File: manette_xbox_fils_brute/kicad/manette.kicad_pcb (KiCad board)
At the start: 2 copper layers, 100 x 53 mm, 25 parts, among them J1 THB001P, J2 THB001P, J3 Conn_01x20, X1 SW_Push, Y1 SW_Push

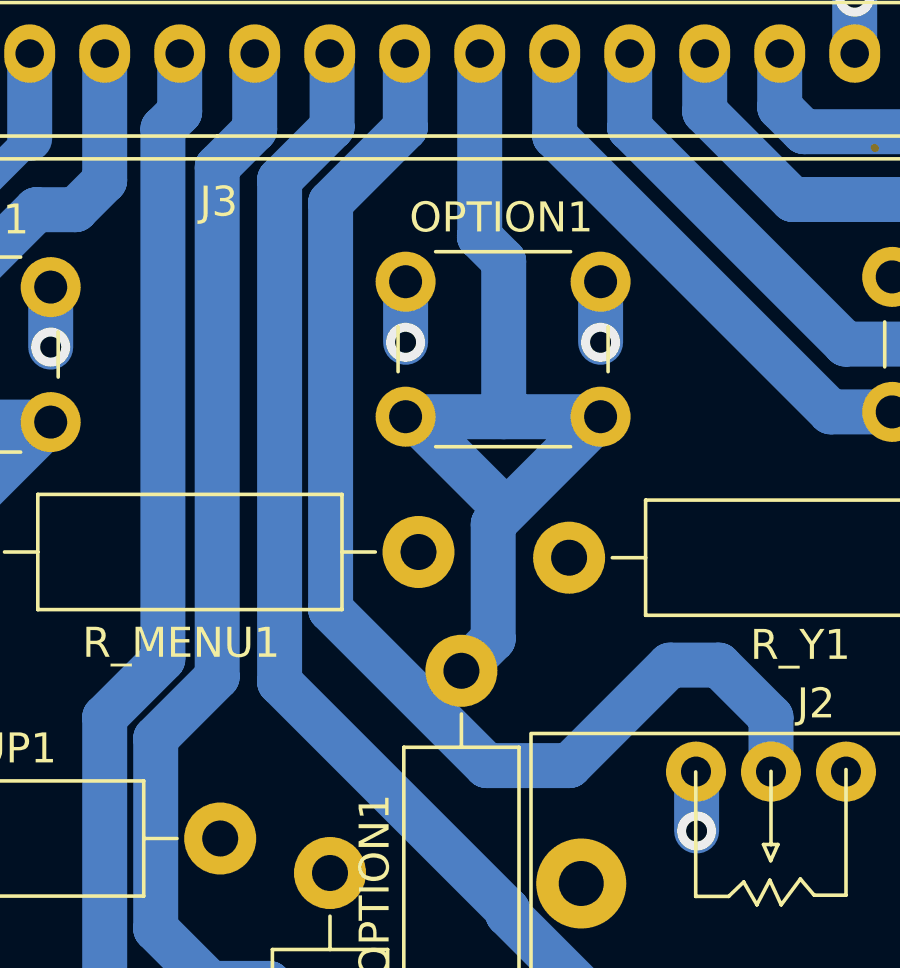
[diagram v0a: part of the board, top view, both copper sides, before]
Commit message: correction fils superposé
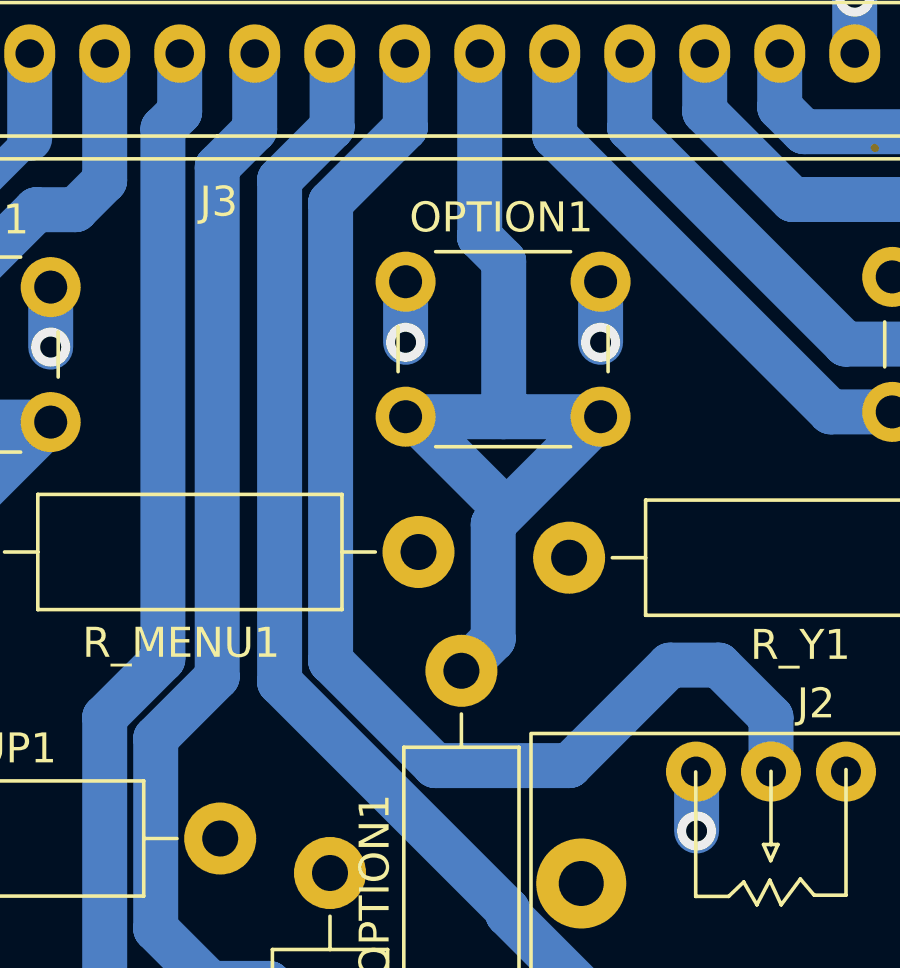
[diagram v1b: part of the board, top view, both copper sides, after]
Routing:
- net JOY_B_X: track 0.00 -> 41.3 mm
- net OPTION: track 73.9 -> 33.5 mm
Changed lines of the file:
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@@
   (segment (start 155.95 95.394164) (end 154.932082 96.412082) (width 1.5) (layer "B.Cu") (net 8))
   (segment (start 159.53 87.984164) (end 156.3 87.984164) (width 1.5) (layer "B.Cu") (net 8))
-  (segment (start 150.53 80.844164) (end 153.02 78.354164) (width 1.5) (layer "B.Cu") (net 8))
   (segment (start 155.5 81.974164) (end 155.5 75.879164) (width 1.5) (layer "B.Cu") (net 8))
-  (segment (start 153.02 78.354164) (end 153.02 75.899164) (width 1.5) (layer "B.Cu") (net 8))
-  (segment (start 158.49 99.614164) (end 155.73 99.614164) (width 1.5) (layer "B.Cu") (net 8))
-  (segment (start 163.47 96.264164) (end 161.84 96.264164) (width 1.5) (layer "B.Cu") (net 8))
   (segment (start 156.3 82.794164) (end 155.49 81.984164) (width 1.5) (layer "B.Cu") (net 8))
-  (segment (start 155.73 99.614164) (end 150.53 94.414164) (width 1.5) (layer "B.Cu") (net 8))
   (segment (start 155.95 91.564164) (end 155.95 95.394164) (width 1.5) (layer "B.Cu") (net 8))
   (segment (start 153.26 87.984164) (end 156.28 91.004164) (width 1.5) (layer "B.Cu") (net 8))
-  (segment (start 161.84 96.264164) (end 158.49 99.614164) (width 1.5) (layer "B.Cu") (net 8))
-  (segment (start 150.53 94.414164) (end 150.53 80.844164) (width 1.5) (layer "B.Cu") (net 8))
   (segment (start 159.53 87.984164) (end 155.95 91.564164) (width 1.5) (layer "B.Cu") (net 8))
-  (segment (start 165.21 98.004164) (end 163.47 96.264164) (width 1.5) (layer "B.Cu") (net 8))
-  (segment (start 165.21 99.814164) (end 165.21 98.004164) (width 1.5) (layer "B.Cu") (net 8))
   (segment (start 156.3 87.984164) (end 153.03 87.984164) (width 1.5) (layer "B.Cu") (net 8))
-  (segment (start 153.02 75.899164) (end 153 75.879164) (width 1.5) (layer "B.Cu") (net 8))
   (segment (start 156.3 87.984164) (end 156.3 82.794164) (width 1.5) (layer "B.Cu") (net 8))
   (segment (start 179.48 77.914164) (end 177.78 77.914164) (width 1.5) (layer "B.Cu") (net 9))
@@
   (segment (start 128.31 82.082996) (end 133 77.392996) (width 1) (layer "B.Cu") (net 15))
   (segment (start 128.31 82.414164) (end 128.31 82.744164) (width 1.5) (layer "B.Cu") (net 15))
+  (segment (start 150.53 80.844164) (end 153.02 78.354164) (width 1.5) (layer "B.Cu") (net 16))
+  (segment (start 165.21 98.004164) (end 163.47 96.264164) (width 1.5) (layer "B.Cu") (net 16))
+  (segment (start 153.02 78.354164) (end 153.02 75.899164) (width 1.5) (layer "B.Cu") (net 16))
+  (segment (start 150.53 96.13) (end 150.53 80.844164) (width 1.5) (layer "B.Cu") (net 16))
+  (segment (start 154.014164 99.614164) (end 150.53 96.13) (width 1.5) (layer "B.Cu") (net 16))
+  (segment (start 158.49 99.614164) (end 154.014164 99.614164) (width 1.5) (layer "B.Cu") (net 16))
+  (segment (start 163.47 96.264164) (end 161.84 96.264164) (width 1.5) (layer "B.Cu") (net 16))
+  (segment (start 165.21 99.814164) (end 165.21 98.004164) (width 1.5) (layer "B.Cu") (net 16))
+  (segment (start 153.02 75.899164) (end 153 75.879164) (width 1.5) (layer "B.Cu") (net 16))
+  (segment (start 161.84 96.264164) (end 158.49 99.614164) (width 1.5) (layer "B.Cu") (net 16))
   (segment (start 150.58 75.959164) (end 150.5 75.879164) (width 1.5) (layer "B.Cu") (net 17))
   (segment (start 156.435 104.439164) (end 148.83 96.834164) (width 1.5) (layer "B.Cu") (net 17))

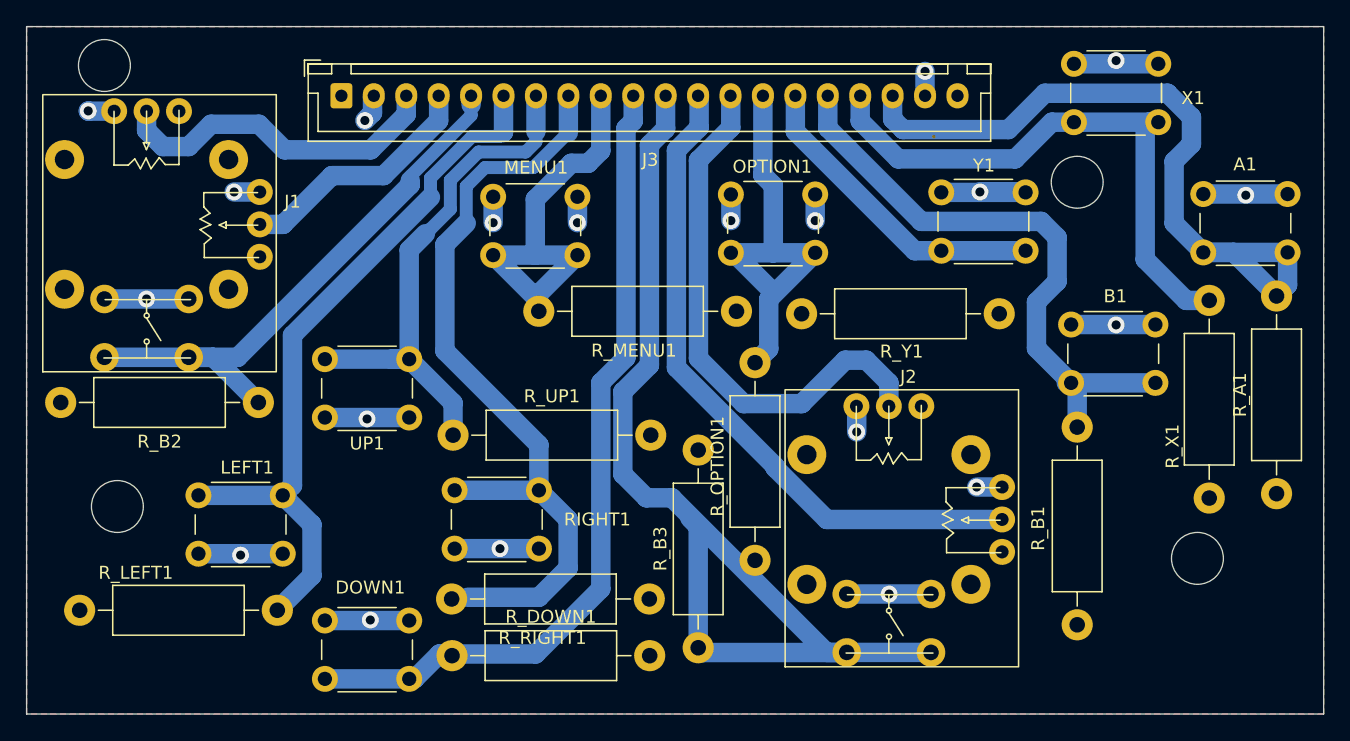
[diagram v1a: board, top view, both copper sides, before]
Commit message: correction erreur & changement forme et trous pcb
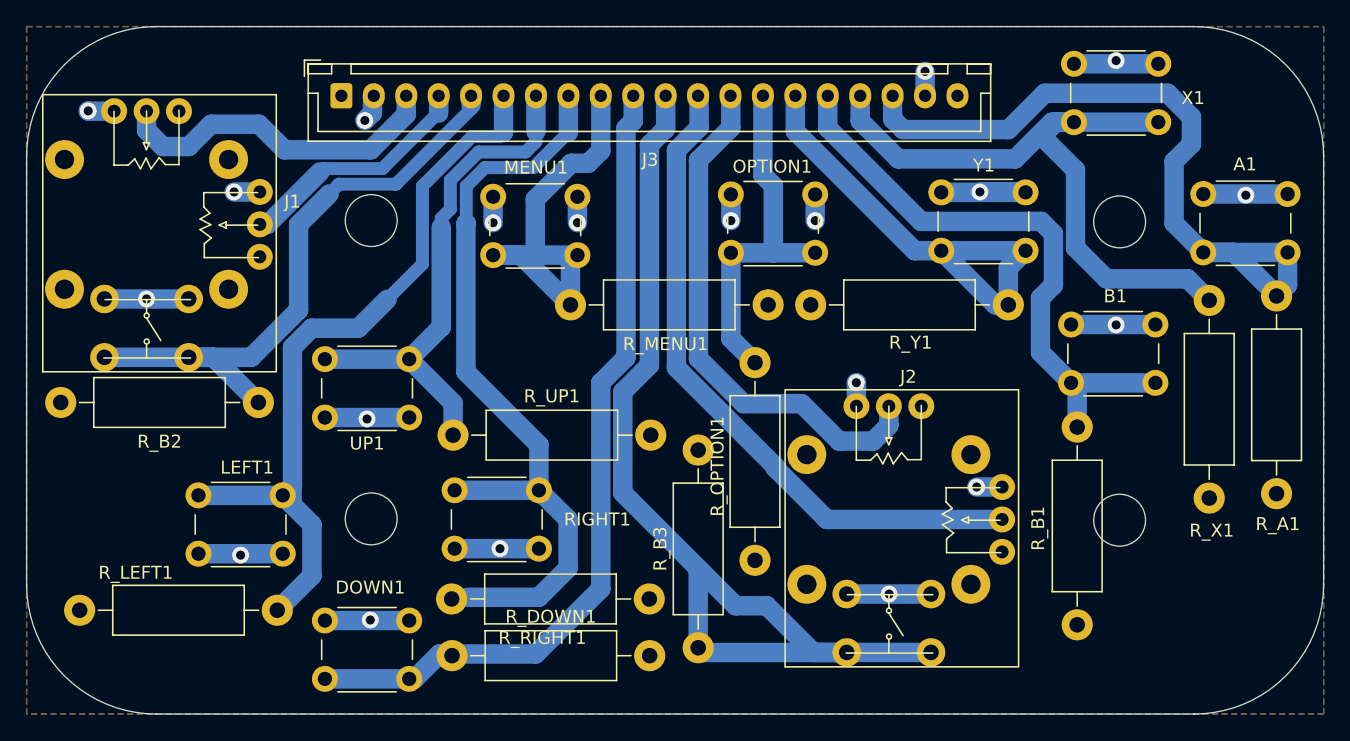
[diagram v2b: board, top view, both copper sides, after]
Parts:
- moved R_MENU1 2.49 mm to (140.7, 92.0)
- moved R_Y1 0.98 mm to (159.2, 92.0)
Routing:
- net Y: track 24.3 -> 35.9 mm
- net X: track 45.0 -> 51.9 mm
- net OPTION: track 33.5 -> 28.2 mm
- net LEFT: track 56.5 -> 60.0 mm
- net JOY_B_A: track 81.9 -> 78.6 mm
- net JOY_A_A: track 44.7 -> 47.9 mm
- net UP: track 41.6 -> 40.2 mm
- net RIGHT: track 61.7 -> 60.3 mm
- net MENU: track 32.0 -> 33.3 mm
- net B: track 47.1 -> 46.3 mm
- net JOY_B_X: track 41.3 -> 40.6 mm
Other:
- outline, holes or cut-outs redrawn
